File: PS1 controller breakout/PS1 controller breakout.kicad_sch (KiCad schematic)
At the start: 3 parts, among them J1 PSX Controller 1P, J2 JST-PH, J3 Conn_01x09_Pin

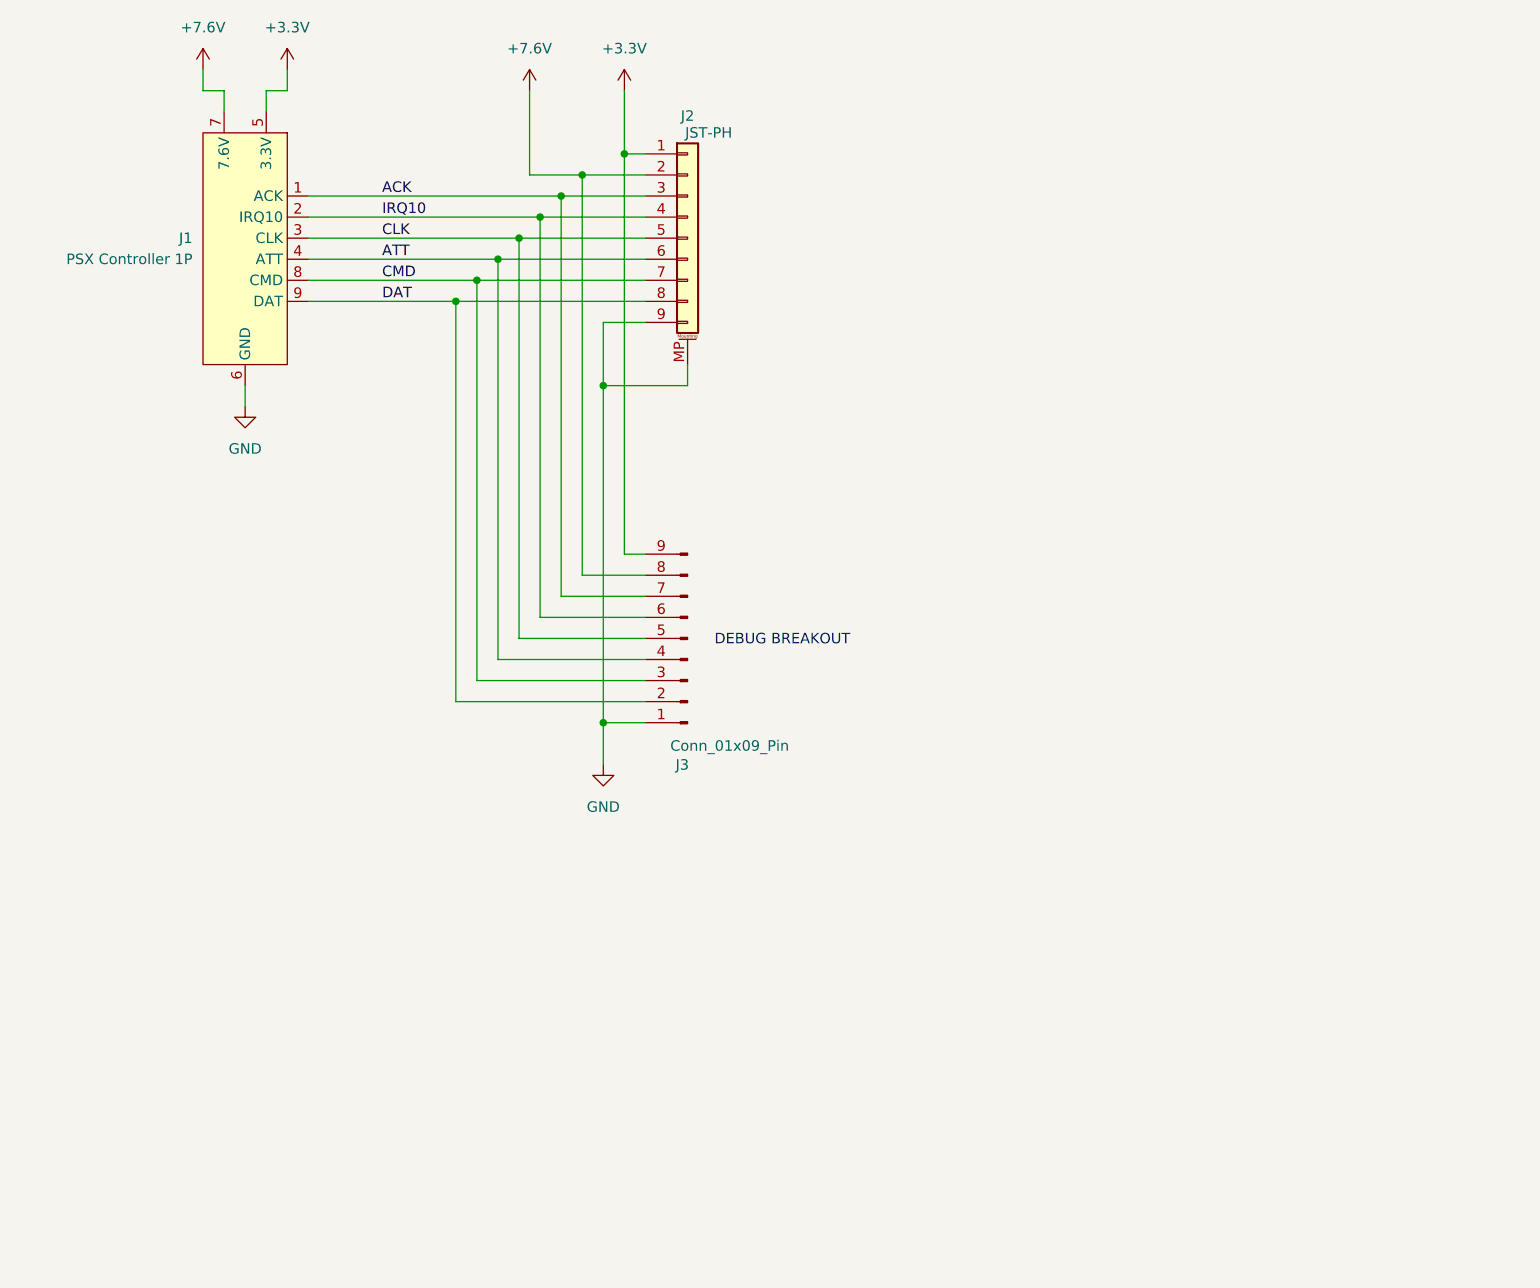
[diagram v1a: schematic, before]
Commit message: Adjusting pinout of JST connector and adding a connector for the P2 controller link
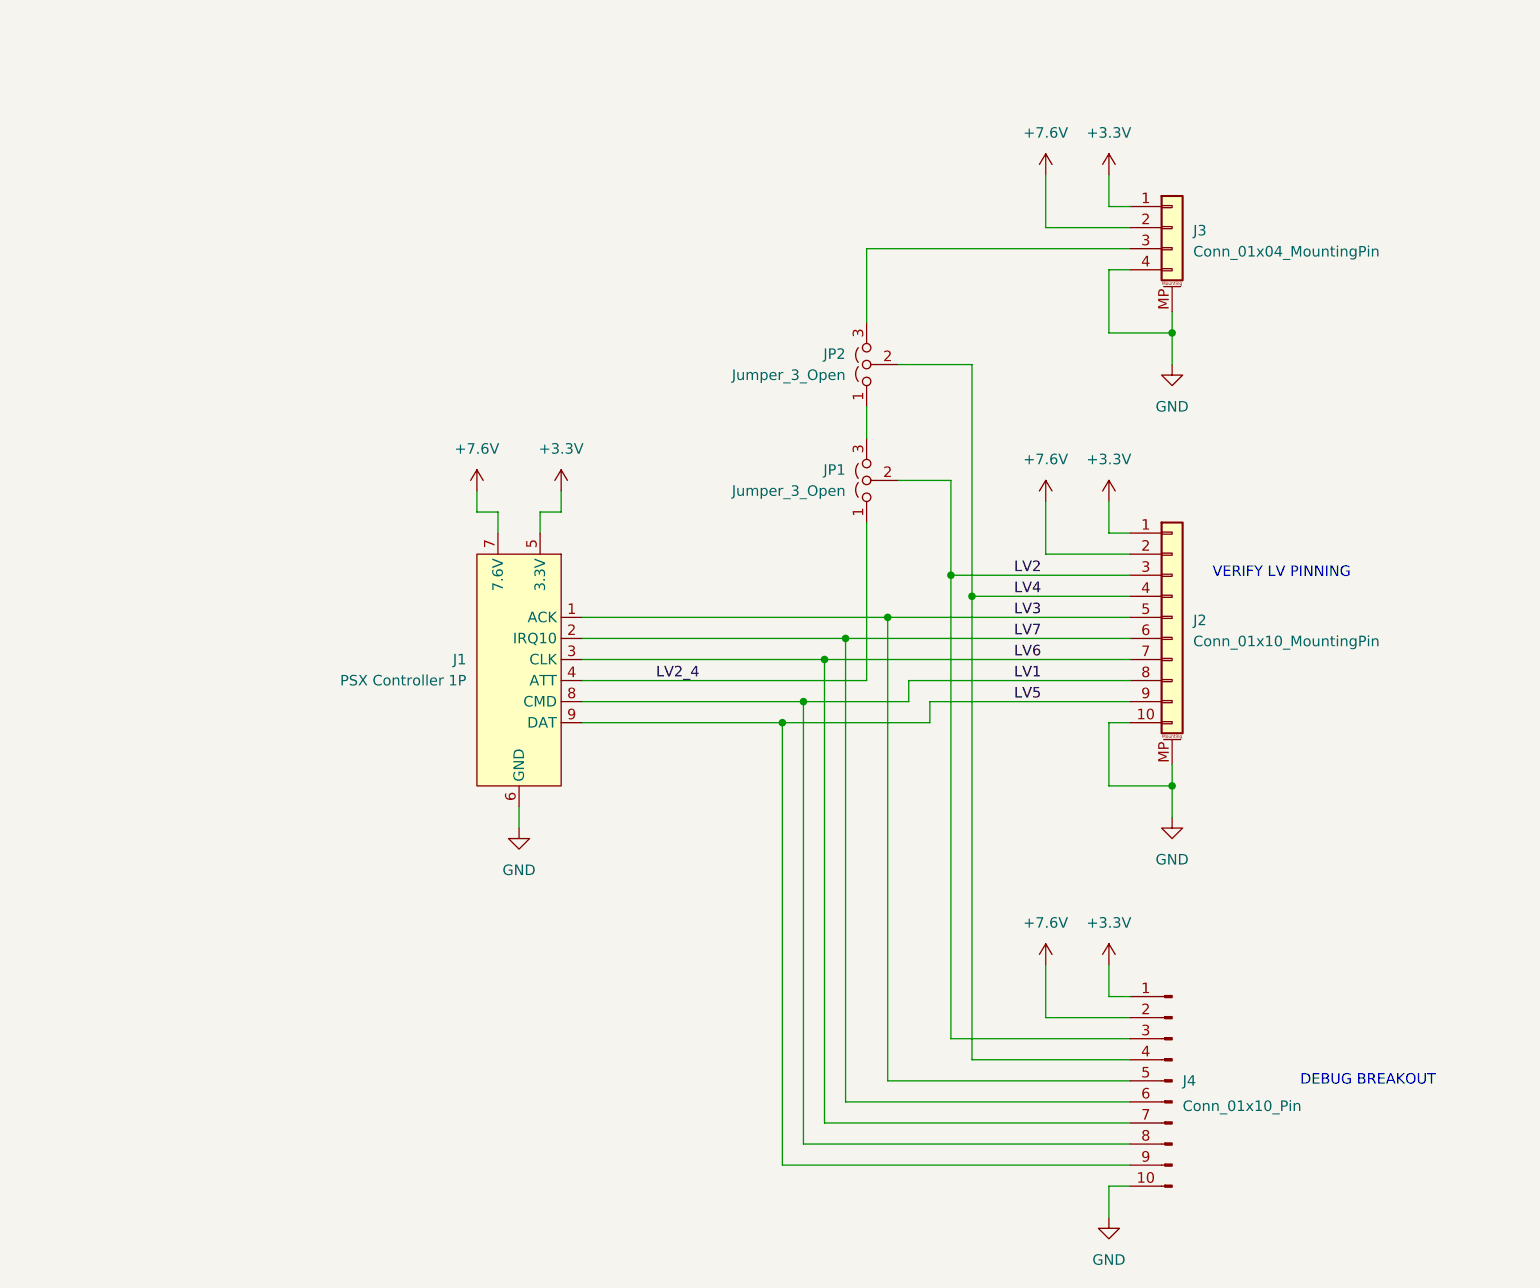
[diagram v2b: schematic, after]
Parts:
- removed J2: JST-PH, Connector_JST:JST_PH_S9B-PH-SM4-TB_1x09-1MP_P2.00mm_Horizontal, symbol Connector_Generic_MountingPin:Conn_01x09_MountingPin
- removed J3: Conn_01x09_Pin, Connector_PinHeader_2.54mm:PinHeader_1x09_P2.54mm_Vertical, symbol Connector:Conn_01x09_Pin
- added J2: Conn_01x10_MountingPin, symbol Connector_Generic_MountingPin:Conn_01x10_MountingPin
- added J3: Conn_01x04_MountingPin, symbol Connector_Generic_MountingPin:Conn_01x04_MountingPin
- added J4: Conn_01x10_Pin, symbol Connector:Conn_01x10_Pin
- added JP1, JP2: Jumper_3_Open, symbol Jumper:Jumper_3_Open
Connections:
- net +3.3V: now also J2.1 (Pin_1), J3.1 (Pin_1), J4.1 (Pin_1)
- net +7.6V: now also J2.2 (Pin_2), J3.2 (Pin_2), J4.2 (Pin_2)
- net GND: now also J2.10 (Pin_10), J2.MP (MountPin), J3.4 (Pin_4), J3.MP (MountPin), J4.10 (Pin_10)
- net ACK renamed LV3
- net LV3: now also J2.5 (Pin_5), J4.5 (Pin_5)
- net ATT renamed LV2_4
- net LV2_4: now also JP1.1 (A)
- net CLK renamed LV6
- net LV6: now also J2.7 (Pin_7), J4.7 (Pin_7)
- net CMD renamed LV1
- net LV1: now also J2.8 (Pin_8), J4.8 (Pin_8)
- net DAT renamed LV5
- net LV5: now also J2.9 (Pin_9), J4.9 (Pin_9)
- net IRQ10 renamed LV7
- net LV7: now also J2.6 (Pin_6), J4.6 (Pin_6)
- new net: J3.3 (Pin_3), JP2.3 (B)
- new net: JP1.3 (B), JP2.1 (A)
- new net LV2: J2.3 (Pin_3), J4.3 (Pin_3), JP1.2 (C)
- new net LV4: J2.4 (Pin_4), J4.4 (Pin_4), JP2.2 (C)
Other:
- note added: "VERIFY LV PINNING"
- moved on the sheet: J1

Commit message: Updated PSX footprint and reoganized JST pinning
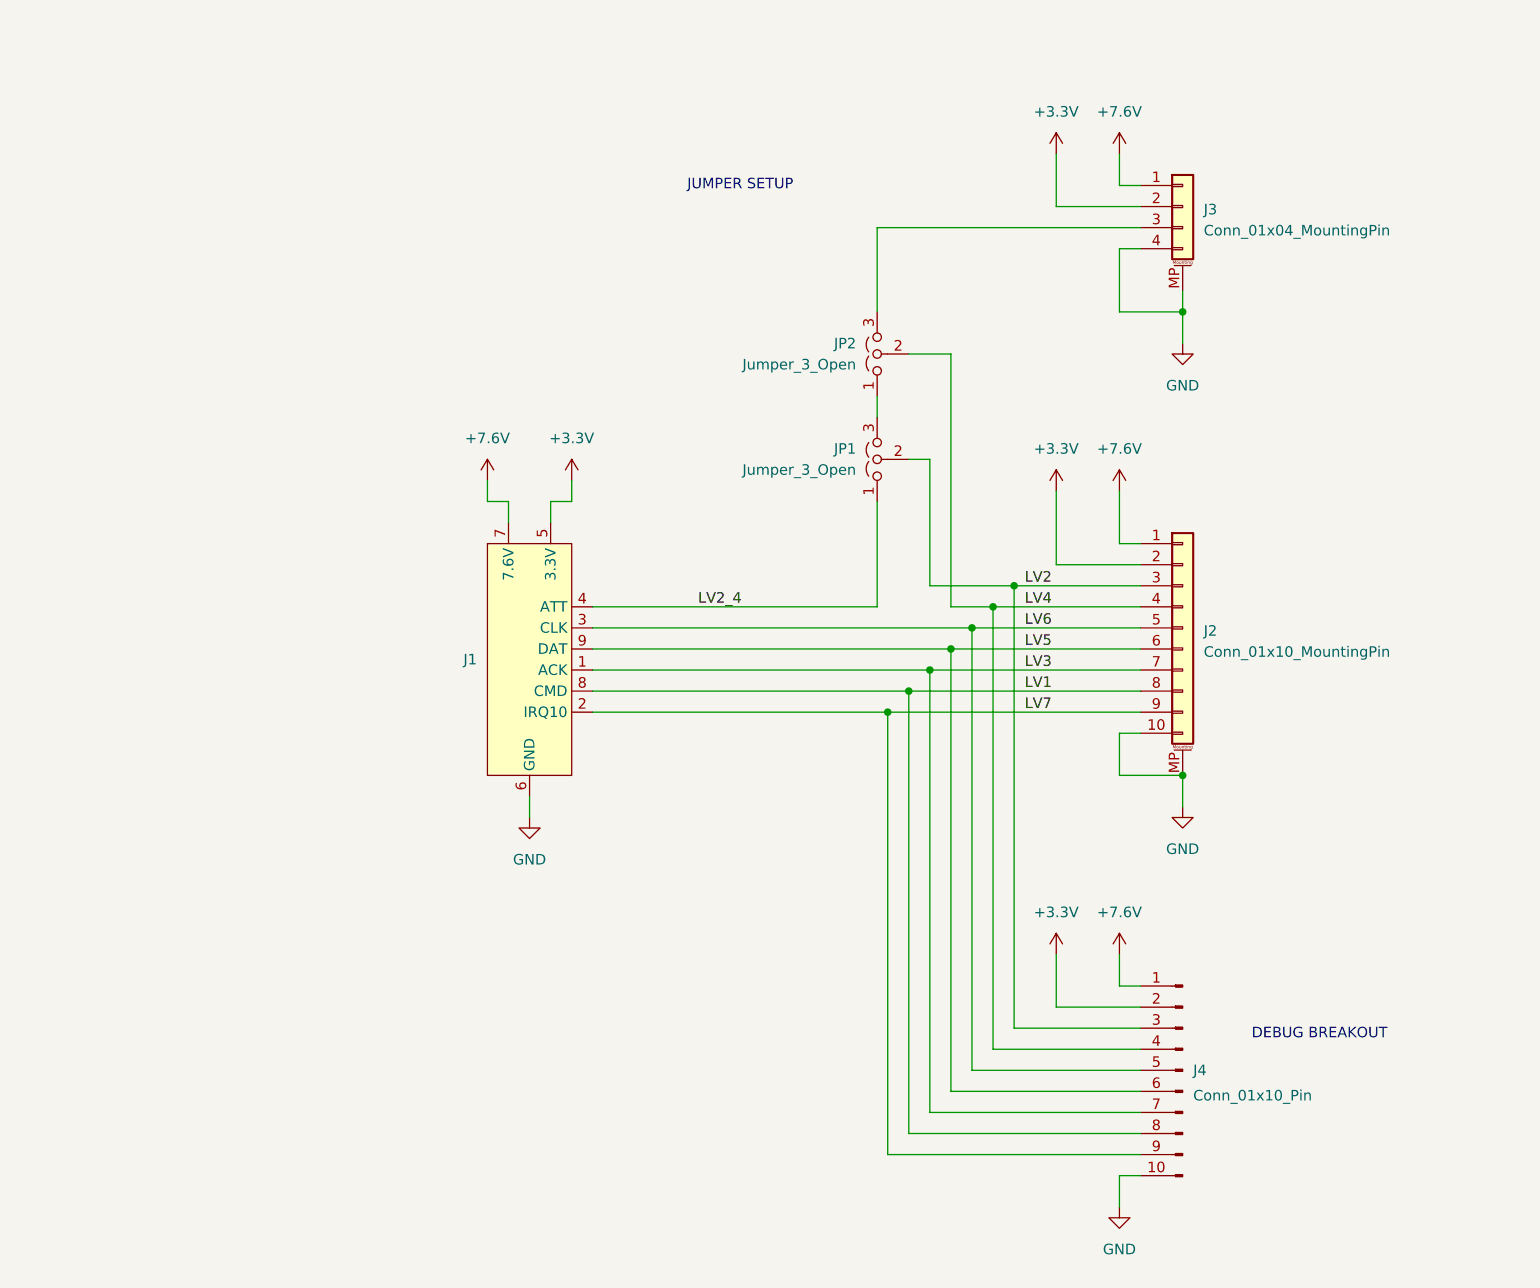
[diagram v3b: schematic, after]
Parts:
- removed J1: PSX Controller 1P, Nick_Connectors:PlayStation 1P, symbol Nick_Connector:PSX Controller 1P
- added J1: (no value), symbol Penny_Connector:PS2_Controller_1P
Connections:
- net +3.3V: now also J2.2 (Pin_2), J3.2 (Pin_2), J4.2 (Pin_2), J1.5 (3.3V); no longer J2.1 (Pin_1), J3.1 (Pin_1), J4.1 (Pin_1)
- net +7.6V: now also J2.1 (Pin_1), J3.1 (Pin_1), J4.1 (Pin_1), J1.7 (7.6V); no longer J2.2 (Pin_2), J3.2 (Pin_2), J4.2 (Pin_2)
- net GND: now also J1.6 (GND)
- net LV1: now also J1.8 (CMD)
- net LV2_4: now also J1.4 (ATT)
- net LV3: now also J2.7 (Pin_7), J4.7 (Pin_7), J1.1 (ACK); no longer J2.5 (Pin_5), J4.5 (Pin_5)
- net LV5: now also J2.6 (Pin_6), J4.6 (Pin_6), J1.9 (DAT); no longer J2.9 (Pin_9), J4.9 (Pin_9)
- net LV6: now also J2.5 (Pin_5), J4.5 (Pin_5), J1.3 (CLK); no longer J2.7 (Pin_7), J4.7 (Pin_7)
- net LV7: now also J2.9 (Pin_9), J4.9 (Pin_9), J1.2 (IRQ10); no longer J2.6 (Pin_6), J4.6 (Pin_6)
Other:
- note added: "JUMPER SETUP"
- note removed: "VERIFY LV PINNING"
- moved on the sheet: J2, J3, J4, JP1, JP2

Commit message: Made Desbug connector DNP and updated descrptive text
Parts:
- J4: now not fitted
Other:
- note added: "DEBUG BREAKOUT SAME PINNING AS JST"
- note removed: "DEBUG BREAKOUT"
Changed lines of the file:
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@@
 		)
 	)
-	(text "DEBUG BREAKOUT"
+	(text "DEBUG BREAKOUT\nSAME PINNING AS JST"
 		(exclude_from_sim no)
-		(at 237.49 170.942 0)
+		(at 249.682 174.498 0)
 		(effects
 			(font
@@
 		(on_board yes)
 		(in_pos_files yes)
-		(dnp no)
+		(dnp yes)
 		(property "Reference" "J4"
 			(at 222.25 175.2599 0)
